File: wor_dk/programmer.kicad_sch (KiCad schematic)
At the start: 44 parts, among them J501 Prog_Ext, J502 USB_C_Receptacle_USB2.0_14P, J503 Prog, Q501 BSS84, SW501 SW_Push, U501 TLV1117-33, U502 LPC11U35FHI33_501, Y501 Crystal

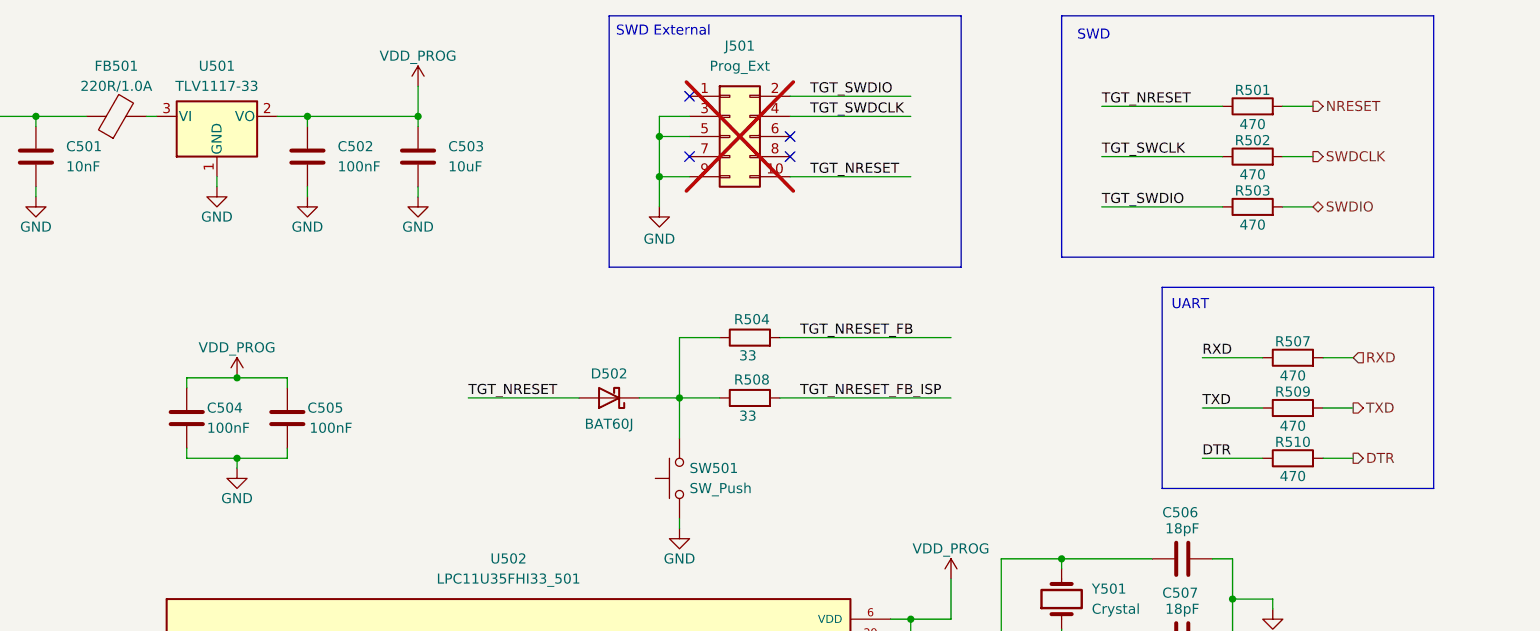
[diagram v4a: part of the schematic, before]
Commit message: wor_dk: top-level connections & cleanup
- top-level connections for TMUX control & UART done (selection
  between FTDI and DAP Link via jumpers)
- all ERC errors & warnings cleaned up
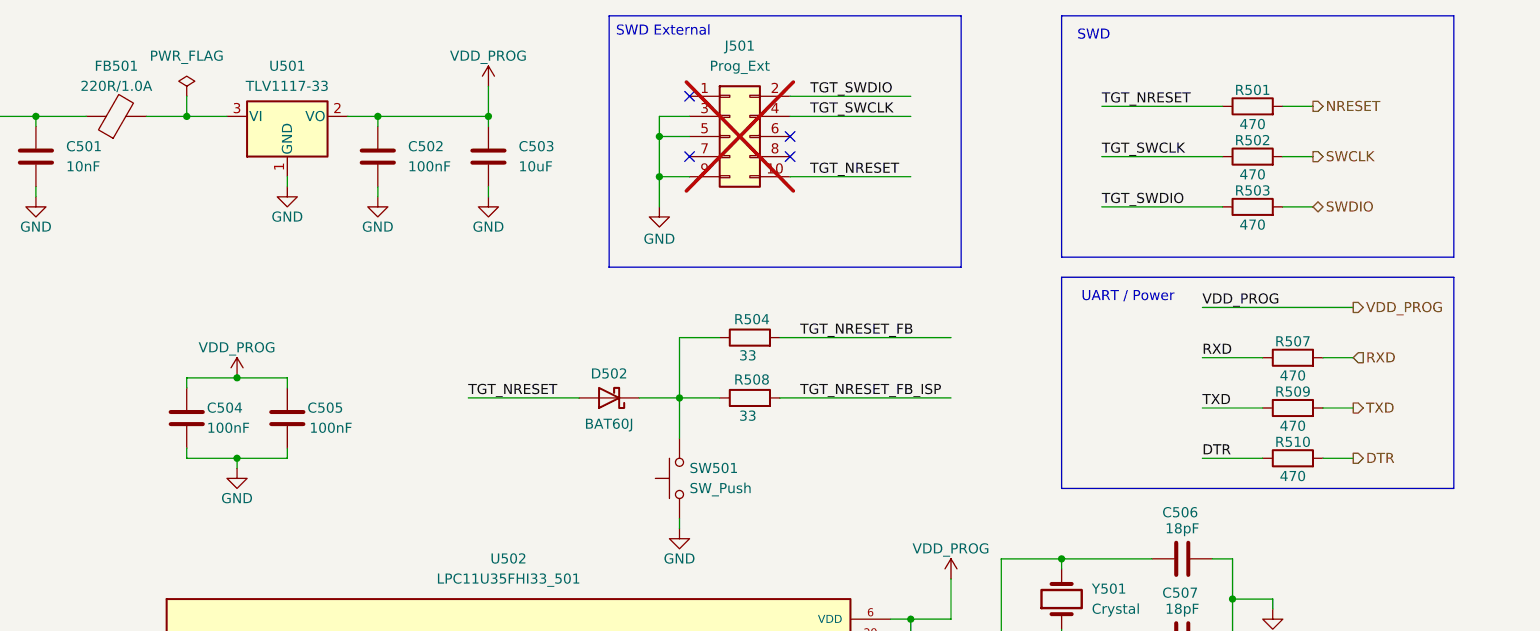
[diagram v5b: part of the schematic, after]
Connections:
- net TGT_SWDCLK is gone; now on net TGT_SWCLK: J501.4 (Pin_4)
- net SWDCLK renamed SWCLK
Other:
- note added: "UART / Power"
- note removed: "UART"
- moved on the sheet: C502, C503, U501

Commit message: wor_dk: add footprints & part info for all resistors
All resistors are JLCPCB basic parts. Footprint 0402 is used for all
resistors, except for 0 Ω resistors, where 0805 is used.
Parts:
- R501, R502, R503, R507, R509, R510: footprint (none) -> Resistor_SMD:R_0402_1005Metric; Comment (none) -> JLCPCB basic part; LCSC (none) -> C25117; MPN (none) -> 0402WGF4700TCE; Manufacturer (none) -> Uniroyal Elec
- R504, R508, R514, R515: footprint (none) -> Resistor_SMD:R_0402_1005Metric; Comment (none) -> JLCPCB basic part; LCSC (none) -> C25105; MPN (none) -> 0402WGF330JTCE; Manufacturer (none) -> Uniroyal Elec
- R505, R506: footprint (none) -> Resistor_SMD:R_0402_1005Metric; Comment (none) -> JLCPCB basic part; LCSC (none) -> C25905; MPN (none) -> 0402WGF5101TCE; Manufacturer (none) -> Uniroyal Elec
- R511: footprint (none) -> Resistor_SMD:R_0805_2012Metric; Comment (none) -> JLCPCB basic part; LCSC (none) -> C17477; MPN (none) -> 0805W8F0000T5E; Manufacturer (none) -> Uniroyal Elec
- R512, R513: footprint (none) -> Resistor_SMD:R_0402_1005Metric; Comment (none) -> JLCPCB basic part; LCSC (none) -> C25744; MPN (none) -> 0402WGF1002TCE; Manufacturer (none) -> Uniroyal Elec
- R516: footprint (none) -> Resistor_SMD:R_0402_1005Metric; Comment (none) -> JLCPCB basic part; LCSC (none) -> C11702; MPN (none) -> 0402WGF1001TCE; Manufacturer (none) -> Uniroyal Elec
- R517, R518, R519: MPN (none) -> 0402WGF2201TCE

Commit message: wor_dk: add footprints & part info for all capacitors
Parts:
- C501: footprint Capacitor_SMD:C_0201_0603Metric -> Capacitor_SMD:C_0805_2012Metric; Comment (none) -> JLCPCB basic part; LCSC C85930 -> C1710; MPN (none) -> CL21B103KBANNNC; Manufacturer Murata Electronics -> Samsung Electro-Mechanics
- C502, C504, C505, C508: MPN (none) -> GRM033R61E104KE14D
- C503: footprint (none) -> Capacitor_SMD:C_0603_1608Metric; Comment (none) -> JLCPCB basic part; LCSC (none) -> C96446; MPN (none) -> CL10A106MA8NRNC; Manufacturer (none) -> Samsung Electro-Mechanics
- C506, C507, C509, C510: footprint (none) -> Capacitor_SMD:C_0603_1608Metric; Comment (none) -> JLCPCB basic part; LCSC (none) -> C1647; MPN (none) -> CL10C180JB8NNNC; Manufacturer (none) -> Samsung Electro-Mechanics

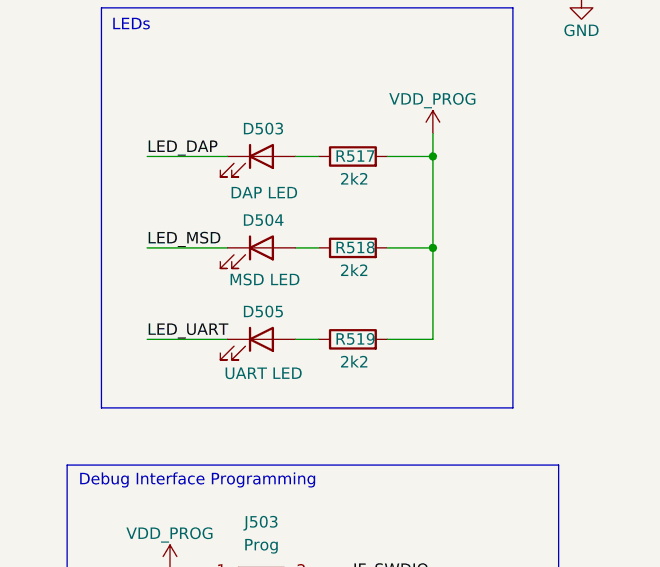
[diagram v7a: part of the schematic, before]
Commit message: wor_dk: add footprints & part info for all diodes & LEDs
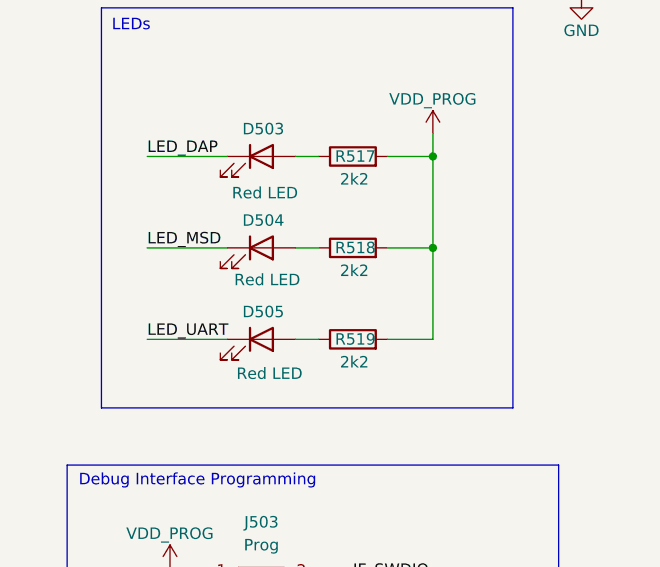
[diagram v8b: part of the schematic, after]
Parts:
- D501: MPN (none) -> PRTR5V0U2X
- D502: footprint (none) -> Diode_SMD:D_SOD-323; LCSC (none) -> C133103; MPN (none) -> BAT60JFILM; Manufacturer (none) -> STMicroelectronics
- D503: value DAP LED -> Red LED; Comment JLCPCB basic part -> DAPLink DAP LED; JLCPCB basic part; MPN (none) -> NCD0805R1
- D504: value MSD LED -> Red LED; Comment JLCPCB basic part -> DAPLink MSD LED; JLCPCB basic part; MPN (none) -> NCD0805R1
- D505: value UART LED -> Red LED; Comment JLCPCB basic part -> DAPLink UART LED; JLCPCB basic part; MPN (none) -> NCD0805R1
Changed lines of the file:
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@@
 			)
 		)
-		(property "Datasheet" "https://assets.nexperia.com/documents/data-sheet/PRTR5V0U2X.pdf"
+		(property "Datasheet" "https://wmsc.lcsc.com/wmsc/upload/file/pdf/v2/lcsc/2108132230_TECH-PUBLIC-PRTR5V0U2X_C2827688.pdf"
 			(at 73.914 59.69 0)
 			(effects
@@
 			)
 		)
-		(property "Description" ""
+		(property "Description" "SOT-143-4 ESD and Surge Protection (TVS/ESD) ROHS"
 			(at 72.39 59.69 0)
 			(effects
@@
 			)
 		)
+		(property "MPN" "PRTR5V0U2X"
+			(at 72.39 59.69 0)
+			(effects
+				(font
+					(size 1.27 1.27)
+				)
+				(hide yes)
+			)
+		)
 		(pin "1"
 		)
@@
 			)
 		)
-		(property "Value" "MSD LED"
+		(property "Value" "Red LED"
 			(at 42.418 138.176 0)
 			(effects
@@
 			)
 		)
-		(property "Description" "Red 0805 Light Emitting Diodes (LED) ROHS"
+		(property "Description" "25mA Colorless transparent lens 67mcd~195mcd -30℃~+85℃ 615nm~630nm Individual diode Red 130° 65mW 1.6V~2.6V 0805 LED Indication - Discrete ROHS"
 			(at 38.1 134.62 0)
 			(effects
@@
 			)
 		)
-		(property "Comment" "JLCPCB basic part"
+		(property "Comment" "DAPLink MSD LED; JLCPCB basic part"
 			(at 38.1 134.62 0)
 			(effects
@@
 			)
 		)
+		(property "MPN" "NCD0805R1"
+			(at 38.1 134.62 0)
+			(effects
+				(font
+					(size 1.27 1.27)
+				)
+				(hide yes)
+			)
+		)
 		(pin "1"
 		)
@@
 			)
 		)
-		(property "Footprint" ""
+		(property "Footprint" "Diode_SMD:D_SOD-323"
 			(at 163.83 62.23 0)
 			(effects
@@
 			)
 		)
-		(property "Datasheet" "~"
+		(property "Datasheet" "https://wmsc.lcsc.com/wmsc/upload/file/pdf/v2/lcsc/1810121610_STMicroelectronics-BAT60JFILM_C133103.pdf"
+			(at 163.83 62.23 0)
+			(effects
+				(font
+					(size 1.27 1.27)
+				)
+				(hide yes)
+			)
+		)
+		(property "Description" "10V 580mV@1A 3A SOD-323 Schottky Diodes ROHS"
+			(at 163.83 62.23 0)
+			(effects
+				(font
+					(size 1.27 1.27)
+				)
+				(hide yes)
+			)
+		)
+		(property "LCSC" "C133103"
+			(at 163.83 62.23 0)
+			(effects
+				(font
+					(size 1.27 1.27)
+				)
+				(hide yes)
+			)
+		)
+		(property "MPN" "BAT60JFILM"
 			(at 163.83 62.23 0)
 			(effects
@@
 			)
 		)
-		(property "Description" "Schottky diode"
+		(property "Manufacturer" "STMicroelectronics"
 			(at 163.83 62.23 0)
 			(effects
@@
 			)
 		)
-		(property "Value" "UART LED"
+		(property "Value" "Red LED"
 			(at 42.672 148.59 0)
 			(effects
@@
 			)
 		)
-		(property "Description" "Red 0805 Light Emitting Diodes (LED) ROHS"
+		(property "Description" "25mA Colorless transparent lens 67mcd~195mcd -30℃~+85℃ 615nm~630nm Individual diode Red 130° 65mW 1.6V~2.6V 0805 LED Indication - Discrete ROHS"
 			(at 38.1 144.78 0)
 			(effects
@@
 			)
 		)
-		(property "Comment" "JLCPCB basic part"
+		(property "Comment" "DAPLink UART LED; JLCPCB basic part"
 			(at 38.1 144.78 0)
 			(effects
@@
 			)
 		)
+		(property "MPN" "NCD0805R1"
+			(at 38.1 144.78 0)
+			(effects
+				(font
+					(size 1.27 1.27)
+				)
+				(hide yes)
+			)
+		)
 		(pin "1"
 		)
@@
 			)
 		)
-		(property "Value" "DAP LED"
+		(property "Value" "Red LED"
 			(at 42.164 128.524 0)
 			(effects
@@
 			)
 		)
-		(property "Description" "Red 0805 Light Emitting Diodes (LED) ROHS"
+		(property "Description" "25mA Colorless transparent lens 67mcd~195mcd -30℃~+85℃ 615nm~630nm Individual diode Red 130° 65mW 1.6V~2.6V 0805 LED Indication - Discrete ROHS"
 			(at 38.1 124.46 0)
 			(effects
@@
 			)
 		)
-		(property "Comment" "JLCPCB basic part"
+		(property "Comment" "DAPLink DAP LED; JLCPCB basic part"
 			(at 38.1 124.46 0)
 			(effects
@@
 			(at 38.1 124.46 0)
 			(effects
+				(font
+					(size 1.27 1.27)
+				)
+				(hide yes)
+			)
+		)
+		(property "MPN" "NCD0805R1"
+			(at 38.1 124.46 0)
+			(effects
